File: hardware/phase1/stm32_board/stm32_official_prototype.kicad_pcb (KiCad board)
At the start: 6 copper layers, 74 parts, among them CN11 Conn_02x36_Odd_Even, CN12 Conn_02x36_Odd_Even, CN14 USB_B_Micro, CN5 Conn_ARM_JTAG_SWD_10, T2 9013, U11 STM32L496ZGTx, U12 STMPS2151STR, U13 USBLC6-2SC6, U6 LD39050PU33R, U8 TSV631AILT, U9 ESDALC6V1W5

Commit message: clean stm32 (ready to order) 2.16.25
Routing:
- net PG4: track 98.5 -> 150.8 mm
- net GND: track 118.9 -> 160.2 mm, vias 43 -> 52
- net PA11: track 106.8 -> 85.3 mm
- net PF6: track 101.8 -> 107.7 mm
- net PF8: track 66.4 -> 62.4 mm
- net PE13: track 61.9 -> 65.3 mm
- net PC13: track 146.3 -> 143.0 mm
- net PF14: track 67.2 -> 64.8 mm
- net VDD: track 308.5 -> 310.9 mm, vias 18 -> 24
- net PG14: track 95.0 -> 92.8 mm
- net PD11: track 196.2 -> 198.2 mm
- net PE1: track 52.9 -> 54.6 mm
- net PE6: track 57.1 -> 58.6 mm
- net PG11: track 81.2 -> 79.7 mm
- net PE7: track 200.5 -> 201.9 mm
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- added copper zone on F.Cu, net GND
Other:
- board outline added: 103.6 x 114 mm
- board text added: "PH3"
- board text removed: "PH3-BOOT0"

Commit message: final manufacturing stm32 version (2.19.25)
im ready.
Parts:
- added REF**: MountingHole_2.1mm, MountingHole:MountingHole_2.1mm, F.Cu at (178.2, 33.6)
- added REF**: MountingHole_2.1mm, MountingHole:MountingHole_2.1mm, F.Cu at (83.2, 33.6)
- added REF**: MountingHole_2.1mm, MountingHole:MountingHole_2.1mm, F.Cu at (178.2, 135.0)
- added REF**: MountingHole_2.1mm, MountingHole:MountingHole_2.1mm, F.Cu at (83.2, 135.0)
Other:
- outline, holes or cut-outs redrawn

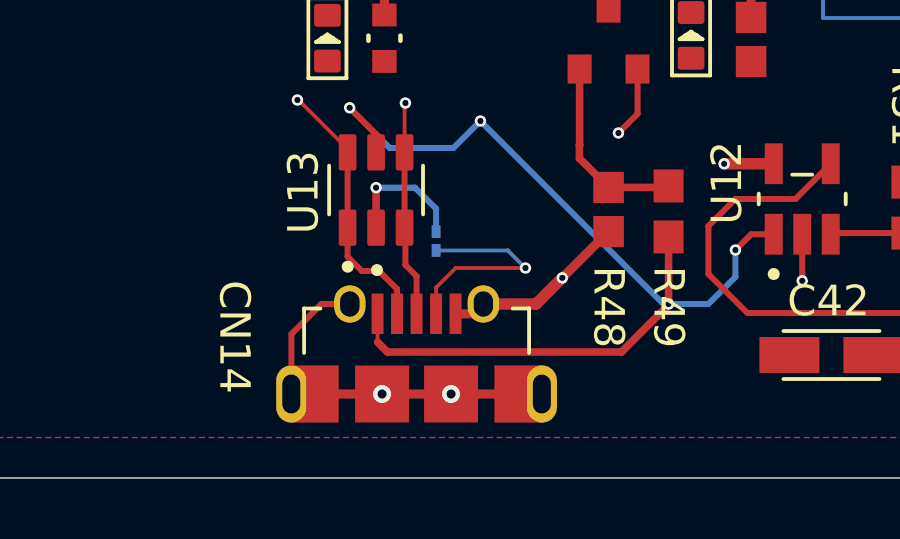
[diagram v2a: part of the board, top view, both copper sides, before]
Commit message: Update STM32 to unconnect uUSB shield from GND
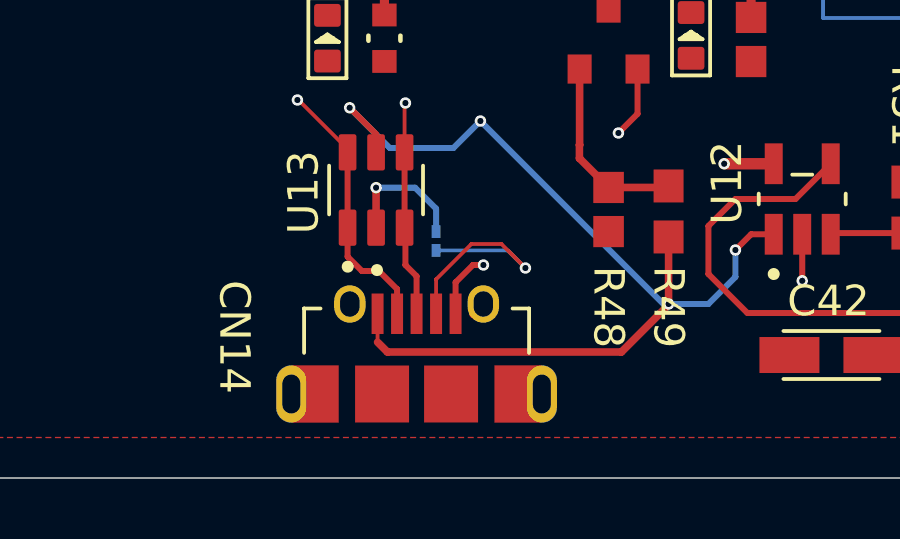
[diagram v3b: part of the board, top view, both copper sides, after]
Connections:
- CN12 pad 7: (no net) -> AVDD
- CN14 pad 10: GND -> (no net)
- CN14 pad 11: GND -> (no net)
- CN14 pad 6: GND -> unconnected-(CN14-Shield-Pad6)
- CN14 pad 7: GND -> (no net)
- CN14 pad 8: GND -> (no net)
- CN14 pad 9: GND -> (no net)
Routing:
- net GND: track 160.2 -> 154.2 mm, vias 52 -> 50
- net PA10: track 249.9 -> 250.7 mm
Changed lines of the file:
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@@
 	(net 155 "IOREF")
 	(net 156 "PG6")
+	(net 157 "unconnected-(CN14-Shield-Pad6)")
 	(footprint "Connector_PinSocket_2.54mm:PinSocket_2x36_P2.54mm_Vertical"
 		(layer "F.Cu")
@@
 			(layers "*.Cu" "*.Mask")
 			(remove_unused_layers no)
+			(net 4 "AVDD")
 			(pinfunction "Pin_7")
 			(pintype "passive")
@@
 			(layers "*.Cu" "*.Mask")
 			(remove_unused_layers no)
-			(net 131 "GND")
+			(net 157 "unconnected-(CN14-Shield-Pad6)")
 			(pinfunction "Shield")
-			(pintype "passive")
+			(pintype "passive+no_connect")
 			(solder_mask_margin 0.0762)
 		)
@@
 			(layers "*.Cu")
 			(remove_unused_layers no)
-			(net 131 "GND")
 		)
 		(pad "8" smd rect
@@
 			(size 1.8 1.9)
 			(layers "F.Cu" "F.Paste" "F.Mask")
-			(net 131 "GND")
 			(solder_mask_margin 0.0762)
 		)
@@
 			(size 1.8 1.9)
 			(layers "F.Cu" "F.Paste" "F.Mask")
-			(net 131 "GND")
 			(solder_mask_margin 0.0762)
 		)
@@
 			(layers "*.Cu")
 			(remove_unused_layers no)
-			(net 131 "GND")
 		)
 		(pad "11" thru_hole oval
@@
 			(layers "*.Cu" "*.Mask")
 			(remove_unused_layers no)
-			(net 131 "GND")
 			(solder_mask_margin 0.0762)
 		)
@@
 	)
 	(gr_line
-		(start 130.4 140.9)
-		(end 127.6 140.9)
-		(stroke
-			(width 0.3048)
-			(type default)
-		)
-		(layer "F.Cu")
-		(net 131)
-	)
-	(gr_line
-		(start 127.6 140.9)
-		(end 122.1 140.9)
-		(stroke
-			(width 0.3048)
-			(type default)
-		)
-		(layer "F.Cu")
-		(net 131)
-	)
-	(gr_line
-		(start 122.1 138.9)
-		(end 122.1 140.9)
-		(stroke
-			(width 0.2)
-			(type default)
-		)
-		(layer "F.Cu")
-		(net 131)
-	)
-	(gr_line
 		(start 146.8 46)
 		(end 151.5 46)
@@
 	)
 	(segment
-		(start 129.9 136.7)
-		(end 127.575125 136.7)
+		(start 128.1 135.9)
+		(end 126.921625 137.078375)
 		(width 0.127)
 		(layer "F.Cu")
@@
 	)
 	(segment
+		(start 126.921625 137.078375)
+		(end 126.921625 138.2285)
+		(width 0.127)
+		(layer "F.Cu")
+		(net 52)
+	)
+	(segment
 		(start 123.4349 57.94877)
 		(end 121.95 59.43367)
@@
 	)
 	(segment
+		(start 129.9 136.7)
+		(end 129.1 135.9)
+		(width 0.127)
+		(layer "F.Cu")
+		(net 52)
+	)
+	(segment
 		(start 121.95 59.43367)
 		(end 121.95 67.65)
@@
 	)
 	(segment
-		(start 127.575125 136.7)
-		(end 126.921625 137.3535)
-		(width 0.127)
-		(layer "F.Cu")
-		(net 52)
-	)
-	(segment
 		(start 177 72.4)
 		(end 177 39.8)
@@
 	)
 	(segment
-		(start 126.921625 137.3535)
-		(end 126.921625 138.2285)
+		(start 129.1 135.9)
+		(end 128.1 135.9)
 		(width 0.127)
 		(layer "F.Cu")
@@
 	)
 	(segment
-		(start 123.1 137.9)
-		(end 124.046625 137.9)
-		(width 0.2032)
-		(layer "F.Cu")
-		(net 131)
-	)
-	(segment
 		(start 173.8 104.2)
 		(end 170.639648 104.2)
@@
 	)
 	(segment
-		(start 127.571625 138.225)
-		(end 128.171625 138.225)
-		(width 0.3048)
-		(layer "F.Cu")
-		(net 131)
-	)
-	(segment
-		(start 130.256624 137.9)
-		(end 131.128312 137.028312)
-		(width 0.381)
-		(layer "F.Cu")
-		(net 131)
-	)
-	(segment
 		(start 117.7 45.665)
 		(end 117.7 47.1)
@@
 	)
 	(segment
-		(start 122.1 138.9)
-		(end 123.1 137.9)
-		(width 0.2032)
-		(layer "F.Cu")
-		(net 131)
-	)
-	(segment
 		(start 128.125001 72.125)
 		(end 128.125001 70.9)
@@
 	)
 	(segment
+		(start 127.571625 137.178375)
+		(end 127.571625 138.225)
+		(width 0.2)
+		(layer "F.Cu")
+		(net 131)
+	)
+	(segment
 		(start 112.6 45.85)
 		(end 112.6 44.5)
@@
 	)
 	(segment
+		(start 128.5 136.6)
+		(end 128.15 136.6)
+		(width 0.2)
+		(layer "F.Cu")
+		(net 131)
+	)
+	(segment
 		(start 128.625 92.4209)
 		(end 128.625 93.375)
@@
 	)
 	(segment
-		(start 131.128312 137.028312)
-		(end 131.228312 136.928312)
-		(width 0.3048)
-		(layer "F.Cu")
-		(net 131)
-	)
-	(segment
 		(start 128.125001 70.9)
 		(end 128.125001 70.525001)
@@
 	)
 	(segment
-		(start 131.228312 136.928312)
-		(end 132.671625 135.485)
-		(width 0.3048)
-		(layer "F.Cu")
-		(net 131)
-	)
-	(segment
 		(start 116.3 85)
 		(end 116.800001 84.499999)
@@
 	)
 	(segment
-		(start 128.496625 137.9)
-		(end 130.256624 137.9)
-		(width 0.381)
+		(start 139.1266 135.575)
+		(end 139.1266 137.1266)
+		(width 0.2032)
 		(layer "F.Cu")
 		(net 131)
 	)
 	(segment
-		(start 139.1266 135.575)
-		(end 139.1266 137.1266)
-		(width 0.2032)
+		(start 128.15 136.6)
+		(end 127.571625 137.178375)
+		(width 0.2)
 		(layer "F.Cu")
 		(net 131)
@@
 	)
 	(via
+		(at 128.5 136.6)
+		(size 0.381)
+		(drill 0.2032)
+		(layers "F.Cu" "B.Cu")
+		(free yes)
+		(net 131)
+	)
+	(via
 		(at 133 132.2)
 		(size 0.381)
@@
 	)
 	(via
-		(at 131.128312 137.028312)
-		(size 0.381)
-		(drill 0.2032)
-		(layers "F.Cu" "B.Cu")
-		(teardrops
-			(best_length_ratio 0.5)
-			(max_length 1)
-			(best_width_ratio 1)
-			(max_width 2)
-			(curve_points 0)
-			(filter_ratio 0.9)
-			(enabled no)
-			(allow_two_segments no)
-			(prefer_zone_connections yes)
-		)
-		(net 131)
-	)
-	(via
 		(at 124.3 101.5)
 		(size 0.381)
@@
 	)
 	(via
-		(at 125.121625 140.9)
-		(size 0.6)
-		(drill 0.3)
-		(layers "F.Cu" "B.Cu")
-		(net 131)
-	)
-	(via
 		(at 145.8 135.4)
 		(size 0.381)
@@
 		(net 131)
 	)
-	(via
-		(at 127.421625 140.9)
-		(size 0.6)
-		(drill 0.3)
-		(layers "F.Cu" "B.Cu")
-		(net 131)
-	)

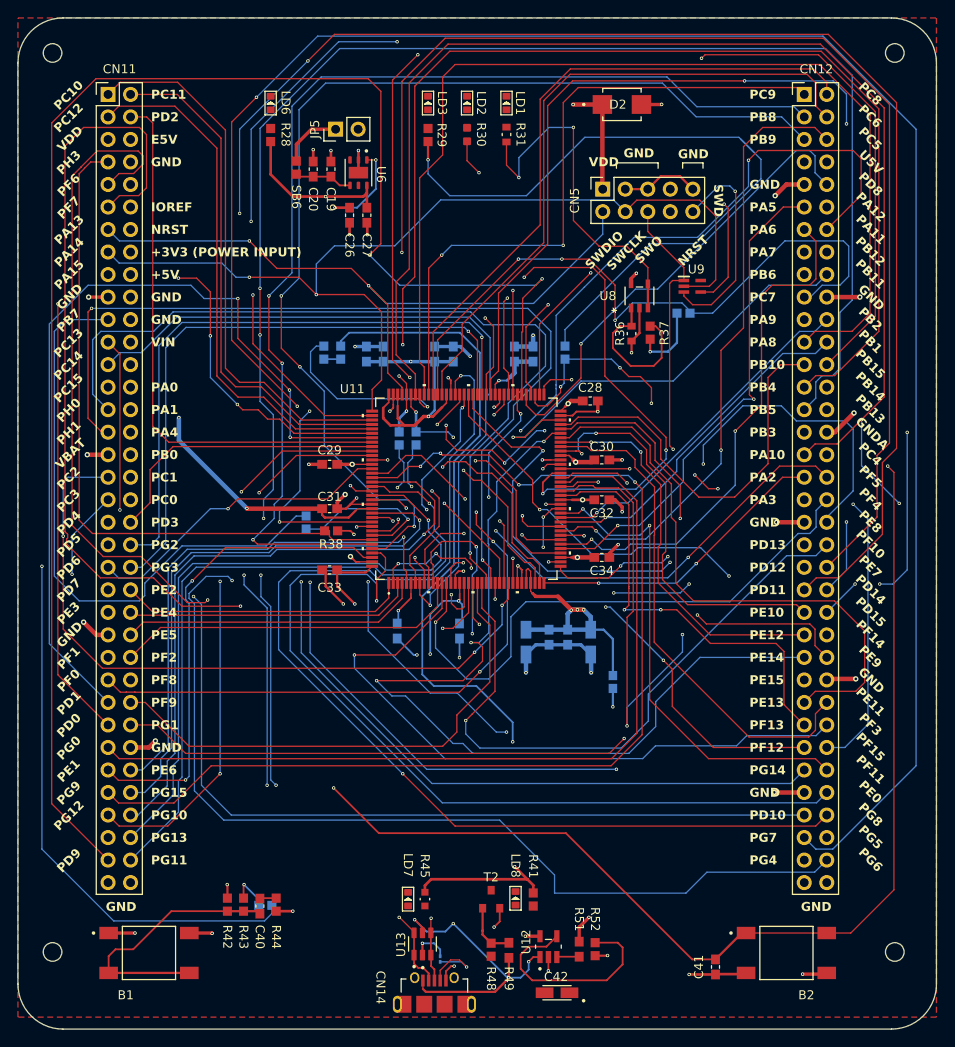
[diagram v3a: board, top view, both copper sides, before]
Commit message: revised final stm32 prototype (2.19.25)
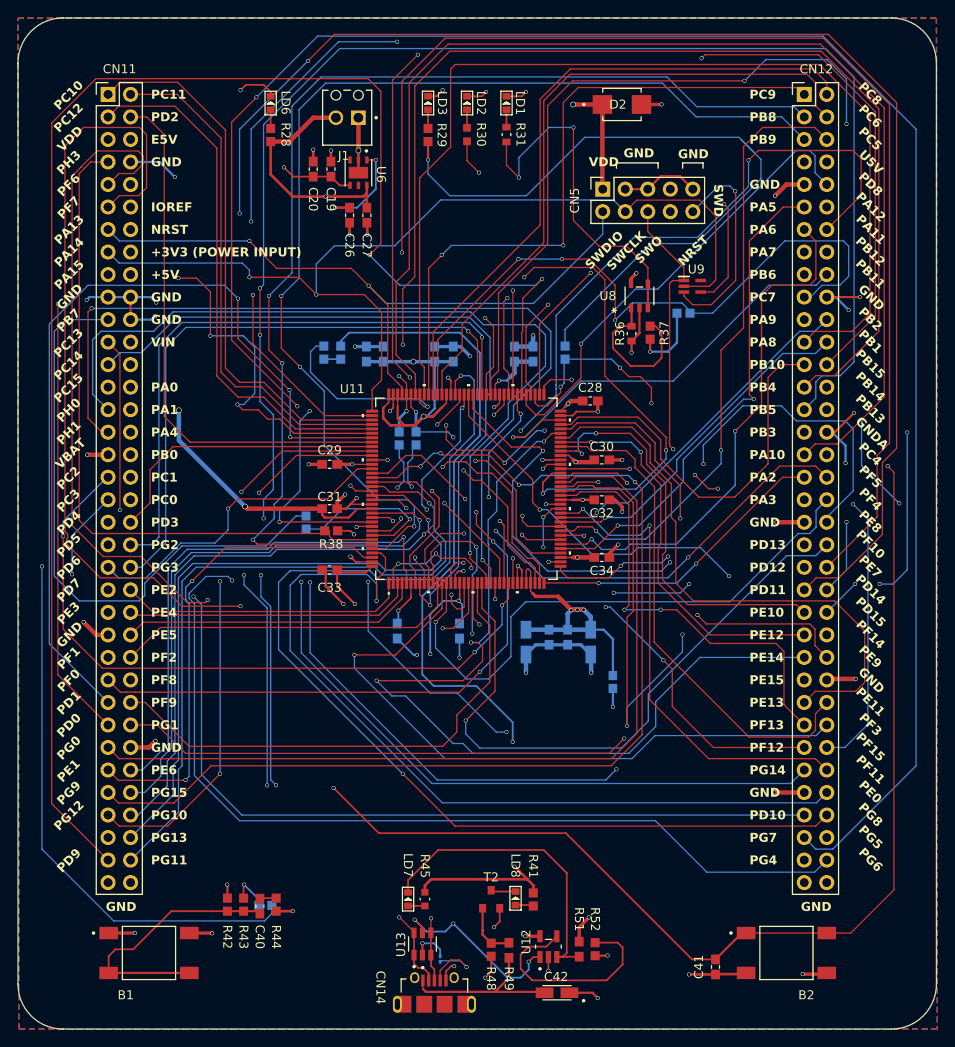
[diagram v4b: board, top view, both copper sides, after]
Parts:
- removed JP5: Conn_01x02_Pin, Connector_PinHeader_2.54mm:PinHeader_1x02_P2.54mm_Vertical
- removed REF** (x4): MountingHole_2.1mm, MountingHole:MountingHole_2.1mm
- removed SB6: Closed, RC0603JR-070RL:RESC1607X60N
- added J1: Screw_Terminal_01x02, 1725656:PHOENIX_1725656, F.Cu at (119.2, 37.8)
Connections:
- C19 pad 1: Net-(U6-VOUT) -> VDD
- C20 pad 1: Net-(U6-VOUT) -> VDD
- U6 pad 4: Net-(U6-VOUT) -> VDD
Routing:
- net GND: track 154.2 -> 200.0 mm, vias 50 -> 61
- net Net-(LD7-K): track 2.48 -> 34.6 mm
- net VDD: track 310.9 -> 319.7 mm, vias 24 -> 25
- net +3V3: track 42.9 -> 51.3 mm
- net Net-(JP5-Pin_1): track 7.03 -> 0.00 mm
- net Net-(U6-VOUT): track 6.18 -> 0.00 mm
- net USB_VBUS: track 129.1 -> 134.8 mm
- net PD0: track 99.4 -> 103.6 mm
- net PG6: track 150.4 -> 146.2 mm
- net PD14: track 132.6 -> 135.6 mm
- net Net-(LD8-K): track 0.00 -> 2.81 mm
- net PC2: track 80.3 -> 77.7 mm
- net Net-(LD3-A): track 0.00 -> 2.11 mm
- net Net-(LD6-A): track 0.00 -> 2.11 mm
- net Net-(LD8-A): track 0.00 -> 2.05 mm
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- added copper zone on B.Cu, net GND
